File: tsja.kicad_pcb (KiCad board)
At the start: 4 copper layers, 95 x 86 mm, 122 parts, among them J1 QWIIC, J10 E-Paper, J2 Micro_SD_Card, J3 SAO, J4 EXT, J6 USB-C, J9 Battery, M1 Vibration, Q1 AP2302B, Q2 AP2302B, Q3 AP2302B, Q4 AO3400 (A09T), Q5 AO3400 (A09T), SW6 SW_SPDT, T1 Select, T2 Start, T3 B, T4 A, T5 Cross, U1 74LVC1G17GW,125, U10 SY6280AAC, U11 SK6805, U12 SK6805, U13 SK6805, U14 SK6805, U15 SK6805, U2 MPR121QR2, U3 ESP32-WROVER-E, U4 TPS63020DSJR, U5 XT4054K421MR-G, U6 SY6280AAC, U7 CH340K, U8 SK6805, U9 SY6280AAC

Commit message: Apply fixes proposed by Paul
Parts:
- added C31: 22u, Capacitor_SMD:C_0805_2012Metric, B.Cu at (-26.3, -12.1)
- moved D21 6.52 mm to (-26.4, -14.1)
- moved D26 5.01 mm to (-38.1, -26.2)
- moved D25 4.81 mm to (-38.1, -28.2), turned to 180 degrees
- moved D27 2.56 mm to (-34.5, -26.9), turned to 90 degrees
- moved C13 1.29 mm to (-36.0, -26.2), turned to 90 degrees
- moved M1 1.03 mm to (-21.1, -10.6)
- moved Q1 1.03 mm to (-26.5, -9.29)
- moved R3 1.03 mm to (-29.0, -6.57)
- moved R9 1.03 mm to (-28.0, -6.57)
- moved R14 0.66 mm to (-14.2, -25.1), turned to -90 degrees
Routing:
- net +3.3V: track 33.1 -> 27.4 mm, vias 16 -> 17
- net VIN: track 78.4 -> 73.1 mm
- net /E-Paper/PREVGL: track 26.3 -> 22.6 mm
- net /E-Paper/PREVGH: track 21.9 -> 18.8 mm
- net Net-(D21-A): track 6.09 -> 8.37 mm
- net Net-(D25-A): track 5.49 -> 4.21 mm
- net GND: track 37.9 -> 38.4 mm, vias 124 -> 206
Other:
- board text added: "Nicolai Electronics & Badge.Team"
- board text added: "Touch me :)"

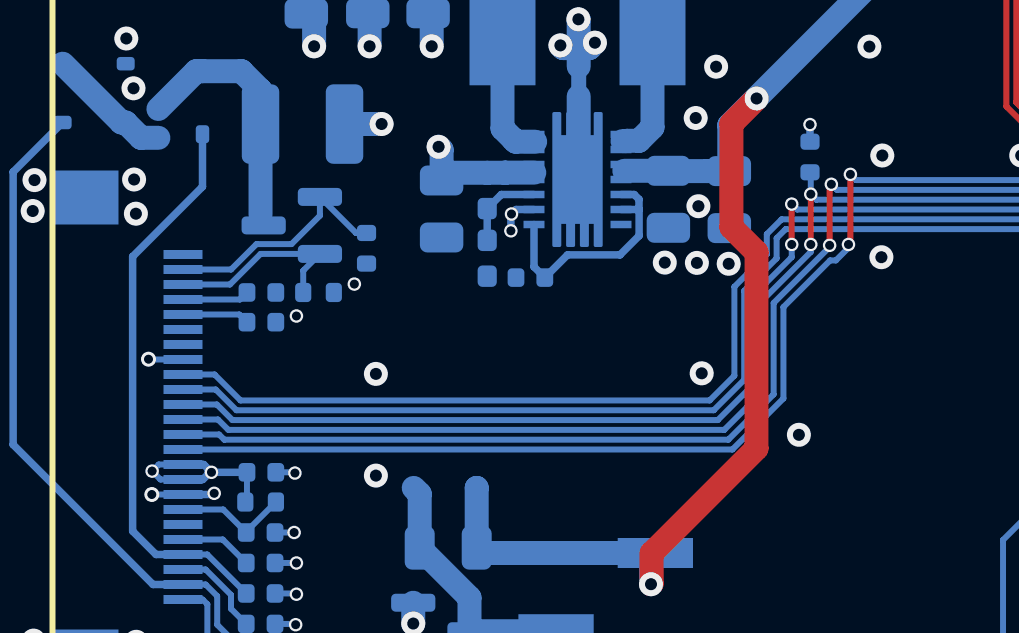
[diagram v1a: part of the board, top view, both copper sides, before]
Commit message: Small fix to ground close to R14
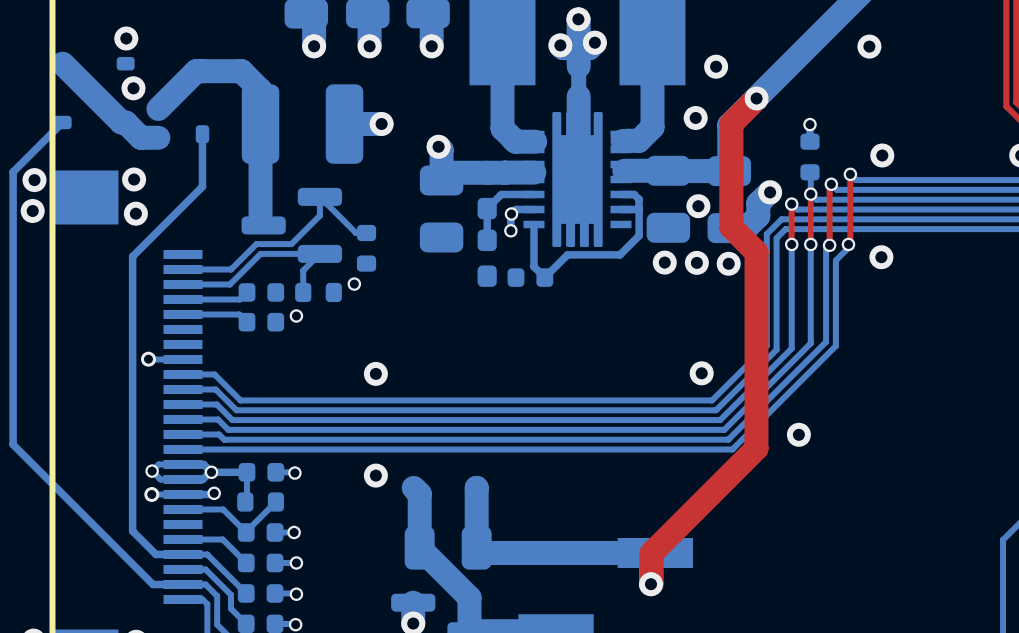
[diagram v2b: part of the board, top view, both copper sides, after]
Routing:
- net GND: track 38.4 -> 40.5 mm, vias 206 -> 207

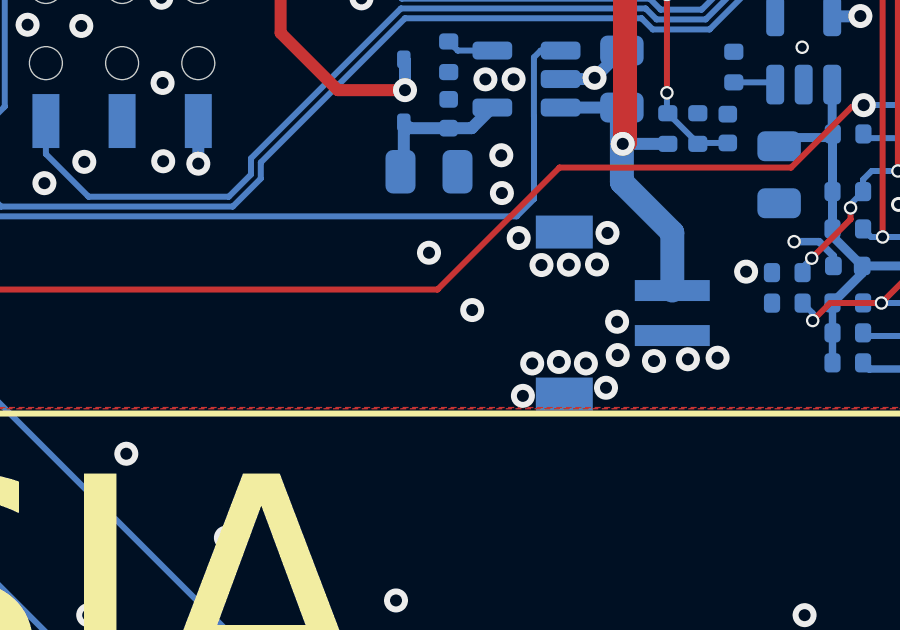
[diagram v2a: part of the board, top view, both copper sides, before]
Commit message: Fill out BOM, add labels to PCB
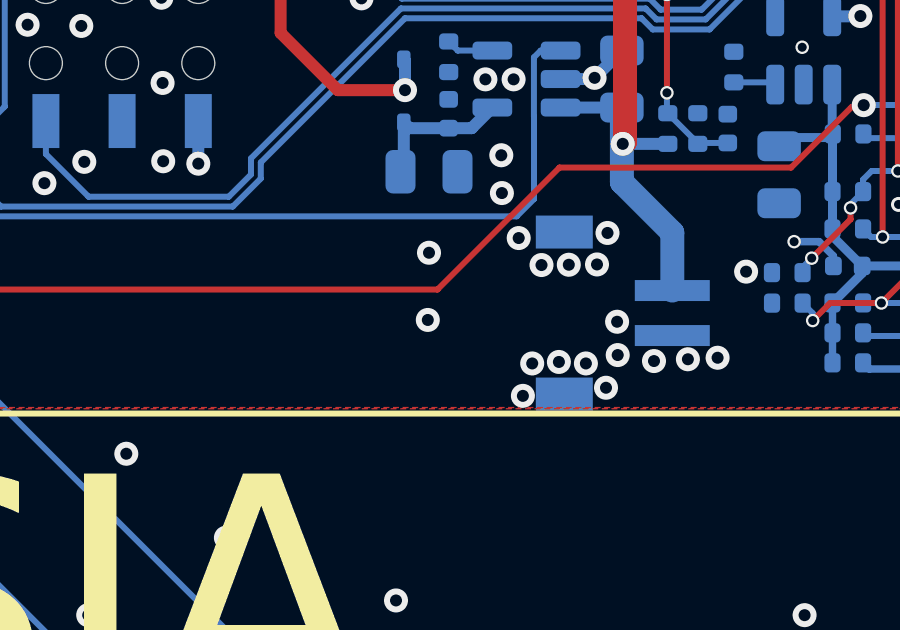
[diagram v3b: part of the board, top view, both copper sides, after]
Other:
- board text added: "BATTERY"
- board text added: "Battery Off-On"
- board text added: "EXPANSION"
- board text added: "SAO"
- board text added: "VIBRATION MOTOR"
